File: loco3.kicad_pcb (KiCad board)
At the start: 2 copper layers, 52 x 42 mm, 4 parts, among them J1 6P6C, J2 6P6C, J3 6P6C, U1 NE555D

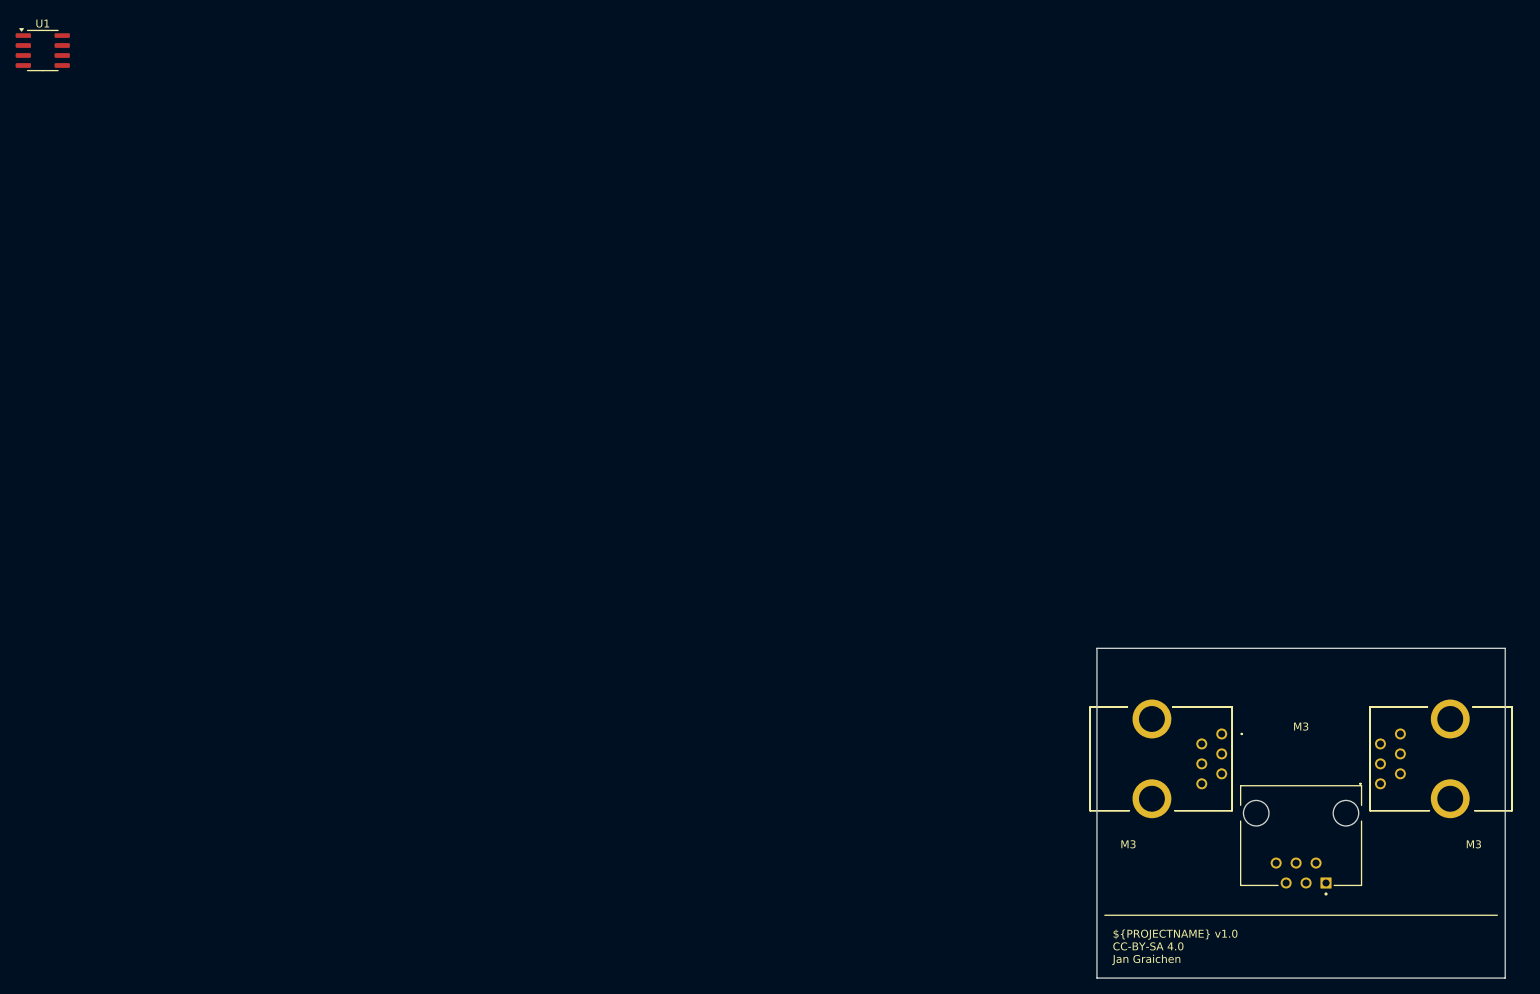
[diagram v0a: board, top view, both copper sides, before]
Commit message: Update WRL export for MCAD
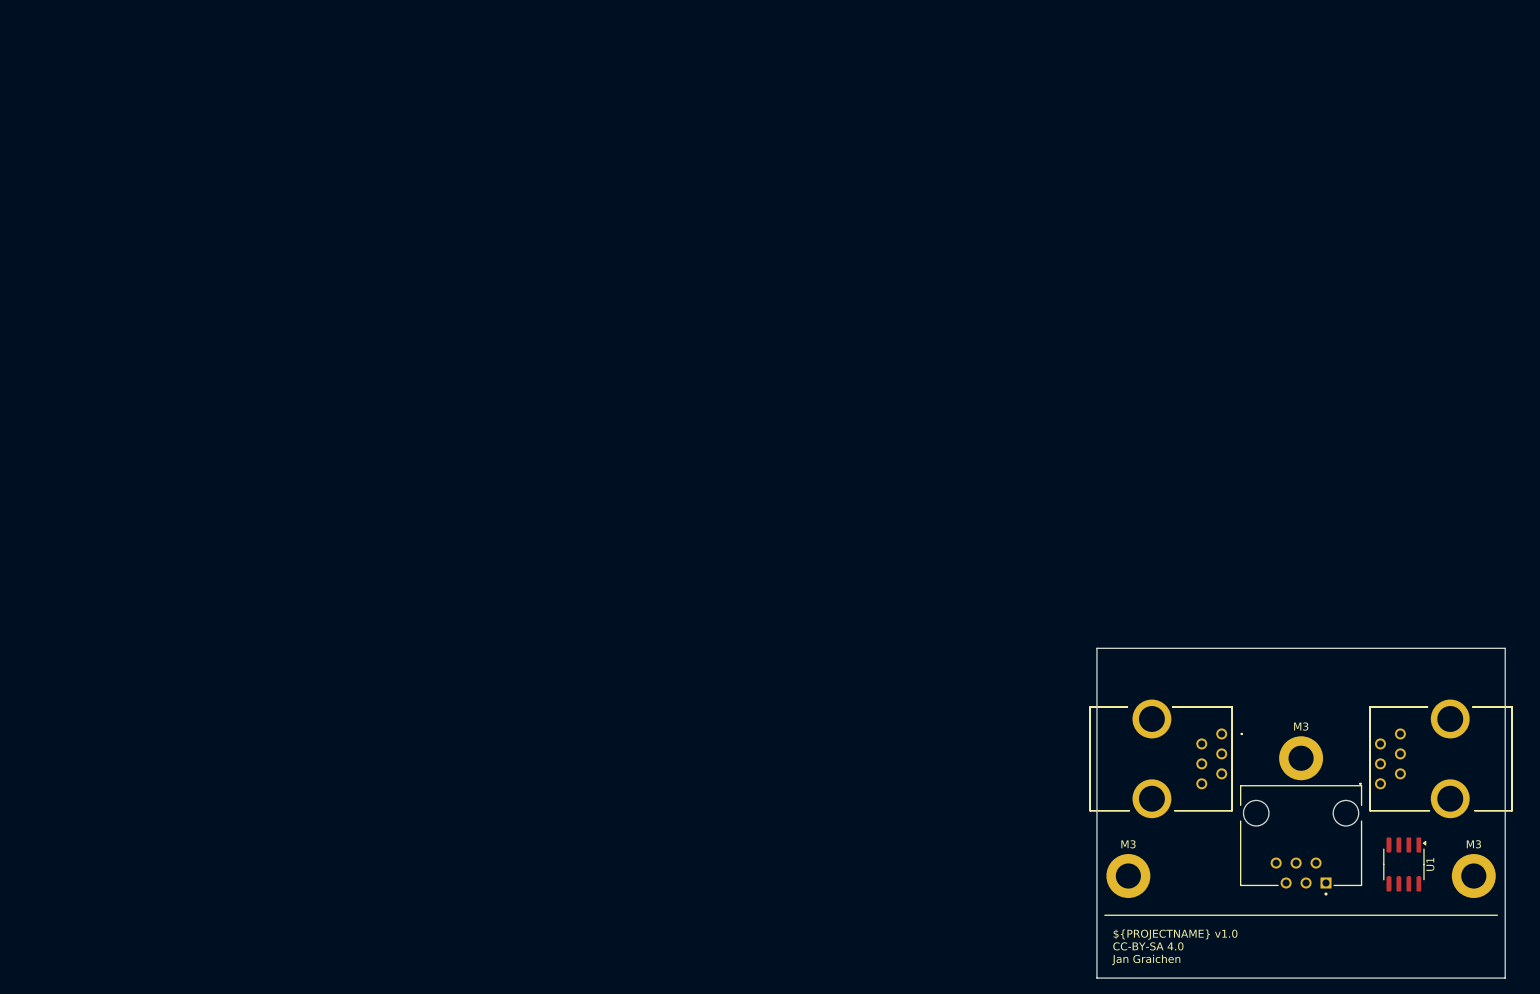
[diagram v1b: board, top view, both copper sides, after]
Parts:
- added REF**: MountingHole_3.2mm_M3_DIN965_Pad, MountingHole:MountingHole_3.2mm_M3_DIN965_Pad, F.Cu at (164.0, 93.0)
- added REF**: MountingHole_3.2mm_M3_DIN965_Pad, MountingHole:MountingHole_3.2mm_M3_DIN965_Pad, F.Cu at (142.0, 108.0)
- added REF**: MountingHole_3.2mm_M3_DIN965_Pad, MountingHole:MountingHole_3.2mm_M3_DIN965_Pad, F.Cu at (186.0, 108.0)
- moved U1 202.0 mm to (177.1, 106.5), turned to -90 degrees

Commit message: WIP
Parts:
- moved REF** 1.00 mm to (143.0, 108.0)
- moved REF** 1.00 mm to (185.0, 108.0)
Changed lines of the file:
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@@
 	(footprint "MountingHole:MountingHole_3.2mm_M3_DIN965_Pad"
 		(layer "F.Cu")
-		(at 142 108)
+		(at 143 108)
 		(descr "Mounting Hole 3.2mm, M3, DIN965")
 		(tags "mounting hole 3.2mm m3 din965")
@@
 	(footprint "MountingHole:MountingHole_3.2mm_M3_DIN965_Pad"
 		(layer "F.Cu")
-		(at 186 108)
+		(at 185 108)
 		(descr "Mounting Hole 3.2mm, M3, DIN965")
 		(tags "mounting hole 3.2mm m3 din965")
@@
 	)
 	(gr_rect
-		(start 139 80)
-		(end 189 120)
+		(start 140 81)
+		(end 188 119)
 		(stroke
 			(width 0.05)
@@
 	)
 	(gr_text "M3"
-		(at 142 104 0)
+		(at 143 104 0)
 		(layer "F.SilkS")
 		(effects
@@
 	)
 	(gr_text "M3"
-		(at 186 104 0)
+		(at 185 104 0)
 		(layer "F.SilkS")
 		(effects

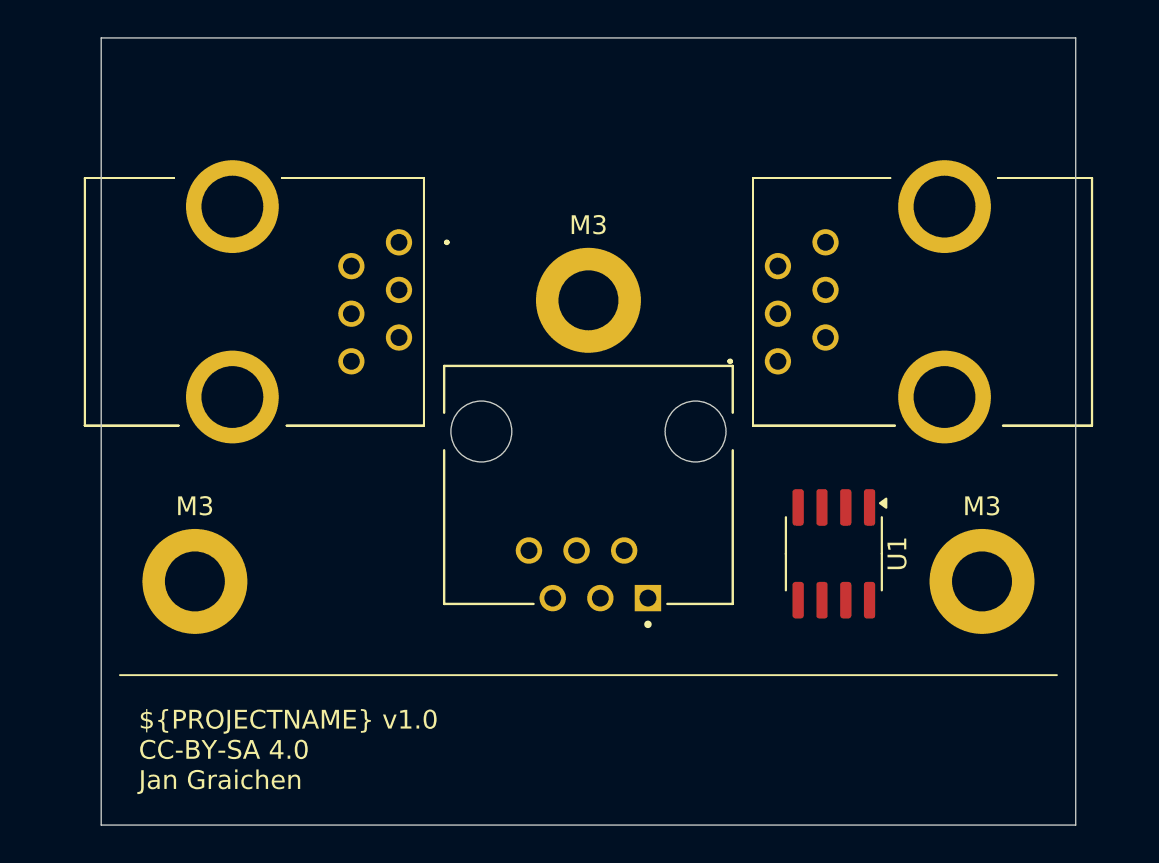
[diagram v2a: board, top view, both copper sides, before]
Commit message: feat: Switch to disable LEDs
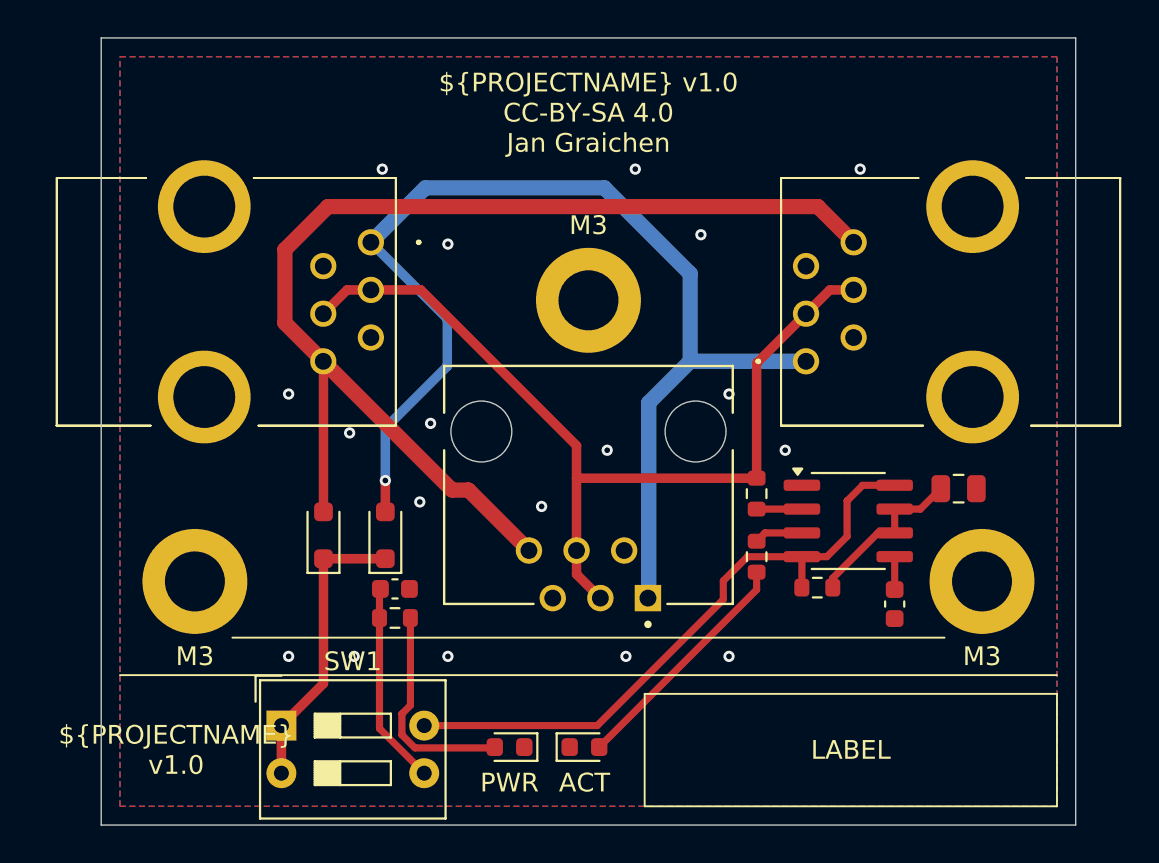
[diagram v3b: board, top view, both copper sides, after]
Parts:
- added C1: 10nF, Capacitor_SMD:C_0603_1608Metric, F.Cu at (180.3, 109.2)
- added C2: 100nF, Capacitor_SMD:C_0603_1608Metric, F.Cu at (153.7, 108.4)
- added C3: 10µF, Capacitor_SMD:C_0805_2012Metric, F.Cu at (183.8, 103.0)
- added D1: BAT54J, Diode_SMD:D_SOD-323_HandSoldering, F.Cu at (153.2, 105.5)
- added D2: BAT54J, Diode_SMD:D_SOD-323_HandSoldering, F.Cu at (149.9, 105.5)
- added D3: PWR, LED_SMD:LED_0603_1608Metric, F.Cu at (159.8, 116.8)
- added D4: ACT, LED_SMD:LED_0603_1608Metric, F.Cu at (163.8, 116.8)
- added R1: 10k, Resistor_SMD:R_0603_1608Metric, F.Cu at (173.0, 103.3)
- added R2: 2k, Resistor_SMD:R_0603_1608Metric, F.Cu at (153.7, 110.0)
- added R3: 2,2k, Resistor_SMD:R_0603_1608Metric, F.Cu at (176.2, 108.3)
- added R4: 2k, Resistor_SMD:R_0603_1608Metric, F.Cu at (173.0, 106.7)
- added SW1: SW_DIP_x02, Button_Switch_THT:SW_DIP_SPSTx02_Slide_9.78x7.26mm_W7.62mm_P2.54mm, F.Cu at (147.6, 115.7)
- moved U1 1.91 mm to (177.9, 104.8), turned to 0 degrees
- moved J1 1.50 mm to (152.4, 89.9)
- moved J3 1.50 mm to (175.6, 96.3)
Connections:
- net VCC renamed Net-(U1-R)
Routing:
- net Net-(D2-A): track 0.00 -> 62.1 mm
- net Net-(D1-A): track 0.00 -> 62.0 mm, vias 0 -> 1
- net Net-(J1-Pad3): track 0.00 -> 48.5 mm
- net Net-(U1-R): track 0.00 -> 33.8 mm
- net VCC: track 0.00 -> 15.7 mm
- net Net-(D4-A): track 0.00 -> 12.8 mm
- net Net-(D3-A): track 0.00 -> 11.7 mm
- net Net-(C2-Pad1): track 0.00 -> 10.8 mm
- net Net-(U1-DIS): track 0.00 -> 8.99 mm
- net Net-(U1-Q): track 0.00 -> 2.60 mm
- net Net-(U1-TR): track 0.00 -> 2.42 mm
- net Net-(U1-CV): track 0.00 -> 1.75 mm
- net GND: vias 0 -> 18
- added copper zone on B.Cu, net GND
- added copper zone on F.Cu, net GND
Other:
- board text added: "${PROJECTNAME} v${REVISION}"
- board text added: "LABEL"

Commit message: WIP
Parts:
- J1, J3: footprint Samacsys:955012611 -> Snapeda:A-2004-1-4-LP-N-R_ASSMANN_A-2004-1-4-LP-N-R
- J2: footprint Snapeda:CUI_CRJ025-1-TH -> Snapeda:A-2014-1-4-N-T-R_ASSMANN_A-2014-1-4-N-T-R
- moved J3 9.16 mm to (184.2, 93.1)
- moved J1 9.11 mm to (143.8, 93.0)
- moved REF** 2.00 mm to (164.0, 91.0)
- moved J2 1.00 mm to (164.0, 101.0)
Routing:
- net Net-(D2-A): track 62.1 -> 63.4 mm
- net Net-(J1-Pad3): track 48.5 -> 49.6 mm
- net GND: vias 18 -> 6

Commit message: WIP
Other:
- board text added: "JLCJLCJLCJLC"

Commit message: feat: Change LED resistors to decrease brightness
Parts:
- R2: value 2k -> 22k
- R4: value 2k -> 27k
